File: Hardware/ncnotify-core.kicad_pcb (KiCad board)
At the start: 4 copper layers, 44 x 21 mm, 44 parts, among them J1 BNC5-J-P-GN-RA-BH2D, J2 Conn_ARM_JTAG_SWD_10, J3 USB4110-GF-A, Q1 NX3008NBKS, SW1 SW_Push, SW2 SW_Push, U1 STM32L422CBT6, U2 TLV71333PDBV, U3 USBLC6-2SC6, U4 USBLC6-2SC6, X1 SMTU1632-LF, Y1 Q13FC1350000400

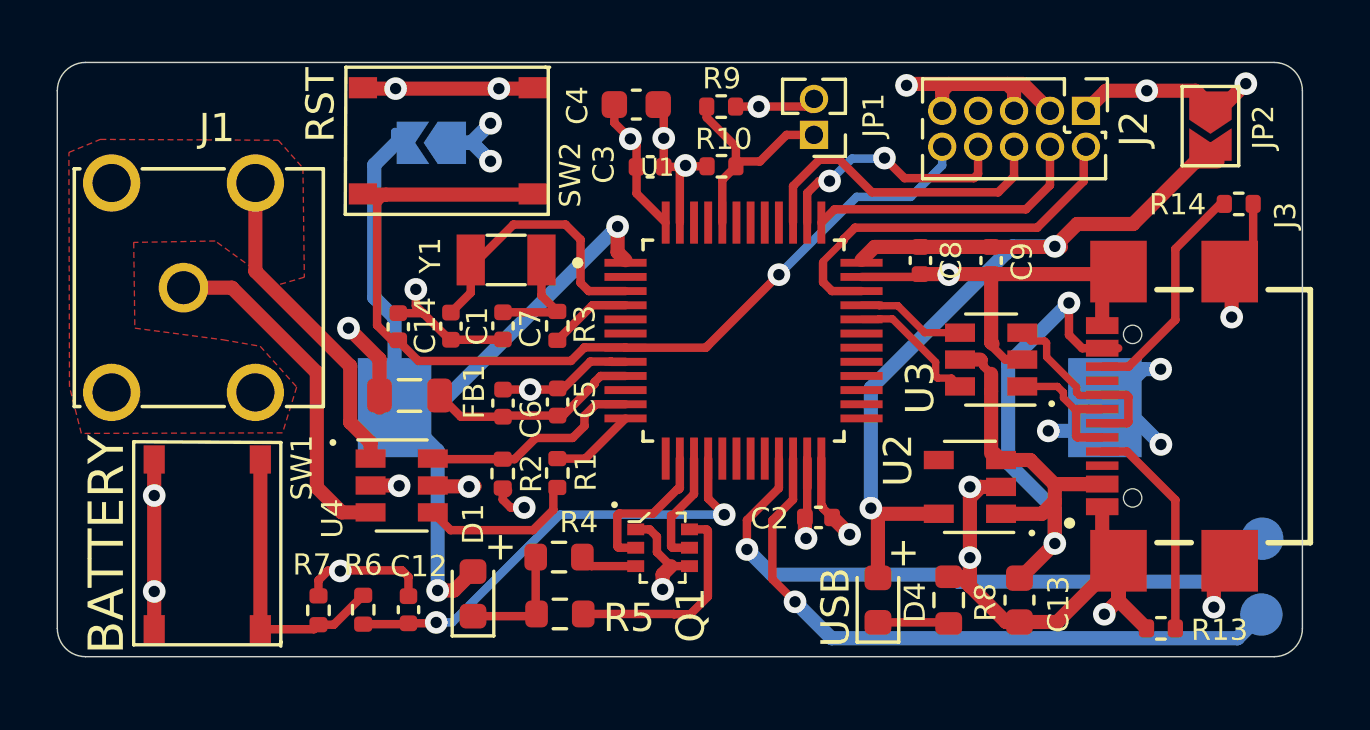
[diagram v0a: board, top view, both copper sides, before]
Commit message: sizeup batt to 2032 for current limit; re-place to fit
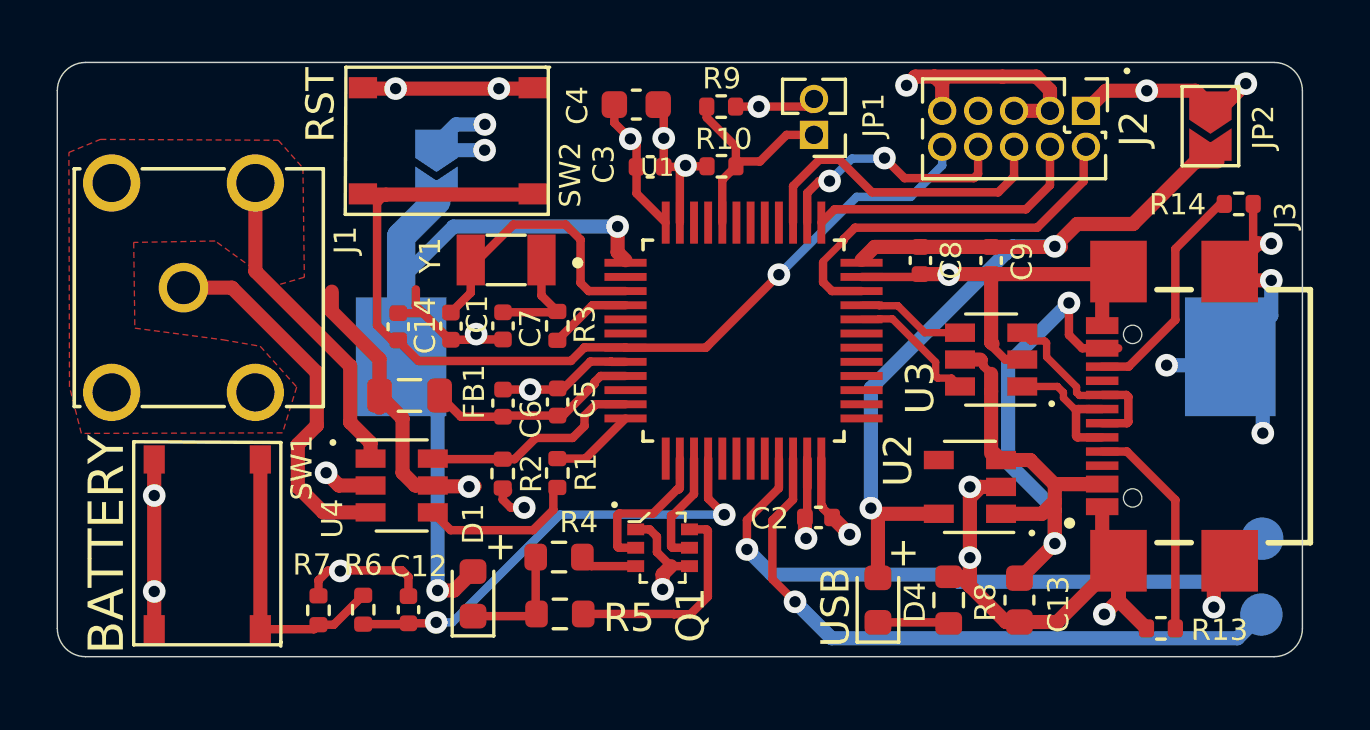
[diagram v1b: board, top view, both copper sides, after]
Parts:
- removed X1: SMTU1632-LF, SamacSys_Parts:SMTU1632LF
- added BT1: BU2032SM-BT-GTR, libs:BAT_BU2032SM-BT-GTR, B.Cu at (235.8, -39.6)
- moved JP3 0.78 mm to (222.4, -46.4), turned to 270 degrees
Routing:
- net GND: track 95.1 -> 104.7 mm
- net VDD: track 32.1 -> 38.4 mm, vias 11 -> 10
- net VBAT: track 31.5 -> 35.2 mm
- net S+: track 12.3 -> 13.2 mm

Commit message: Resolve TH conflicts; add 3d models
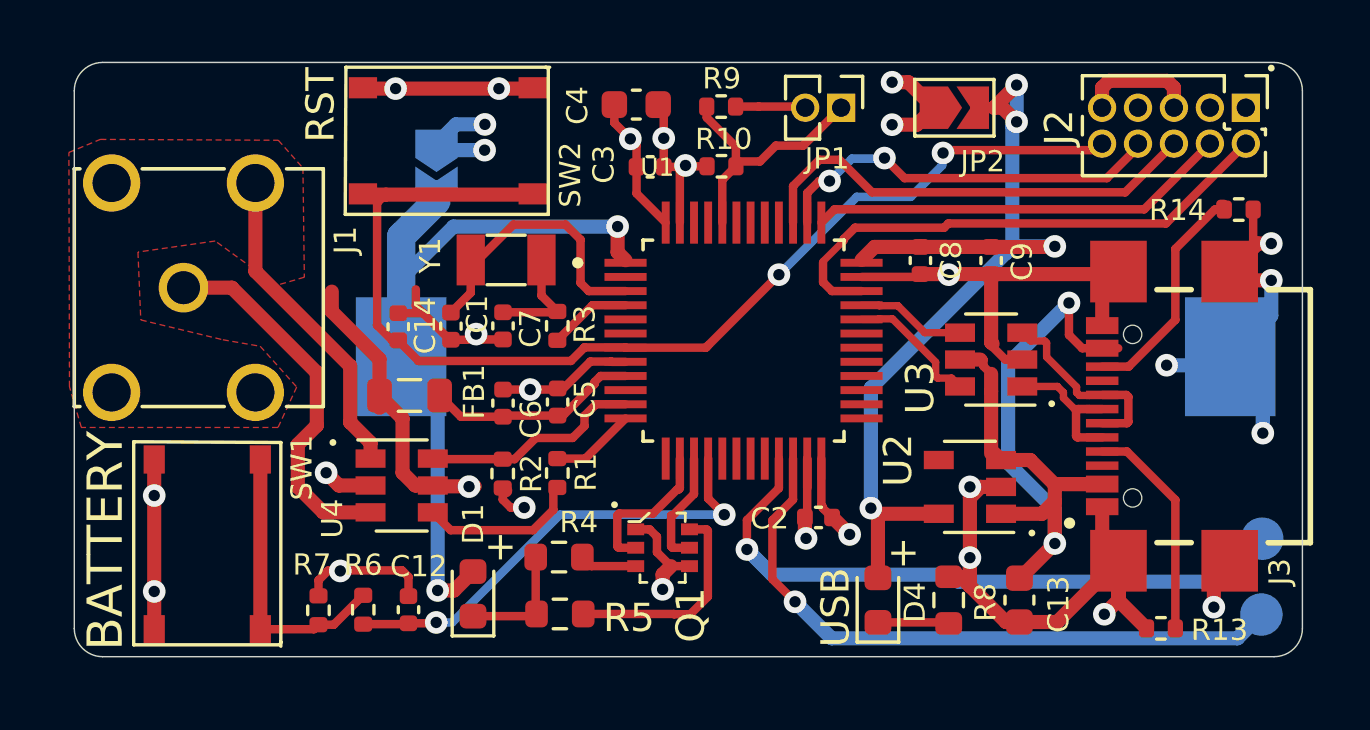
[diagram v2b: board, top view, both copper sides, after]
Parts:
- moved JP2 9.07 mm to (240.7, -48.4), turned to 0 degrees
- moved J2 5.65 mm to (251.0, -48.4)
- moved JP1 1.36 mm to (236.7, -48.4), turned to 270 degrees
- moved R14 0.20 mm to (250.8, -44.8)
- turned BT1 to 0 degrees
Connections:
- BT1 pad +: GND -> VBAT
- BT1 pad -: VBAT -> GND
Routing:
- net NRST: track 34.9 -> 40.6 mm, vias 1 -> 2
- net JTMS-SWDIO: track 13.6 -> 18.9 mm
- net JTDI: track 8.91 -> 14.1 mm
- net JTCK-SWCLK: track 9.73 -> 14.9 mm
- net JTDO: track 11.2 -> 16.3 mm
- net GND: track 104.7 -> 99.6 mm, vias 21 -> 20
- net VDD: track 38.4 -> 35.0 mm, vias 10 -> 9
- net Net-(JP1-Pad1): track 7.84 -> 9.20 mm
- net VBUS: track 33.6 -> 33.5 mm, vias 2 -> 4
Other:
- board size 44 x 21 mm -> 43.4 x 21 mm
- board text added: "v1.1 NCNotify Data Logger Bowen Shaner"
- board text removed: "NCNotify Data Logger v1.1 Bowen Shaner"

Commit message: micro-usb connector
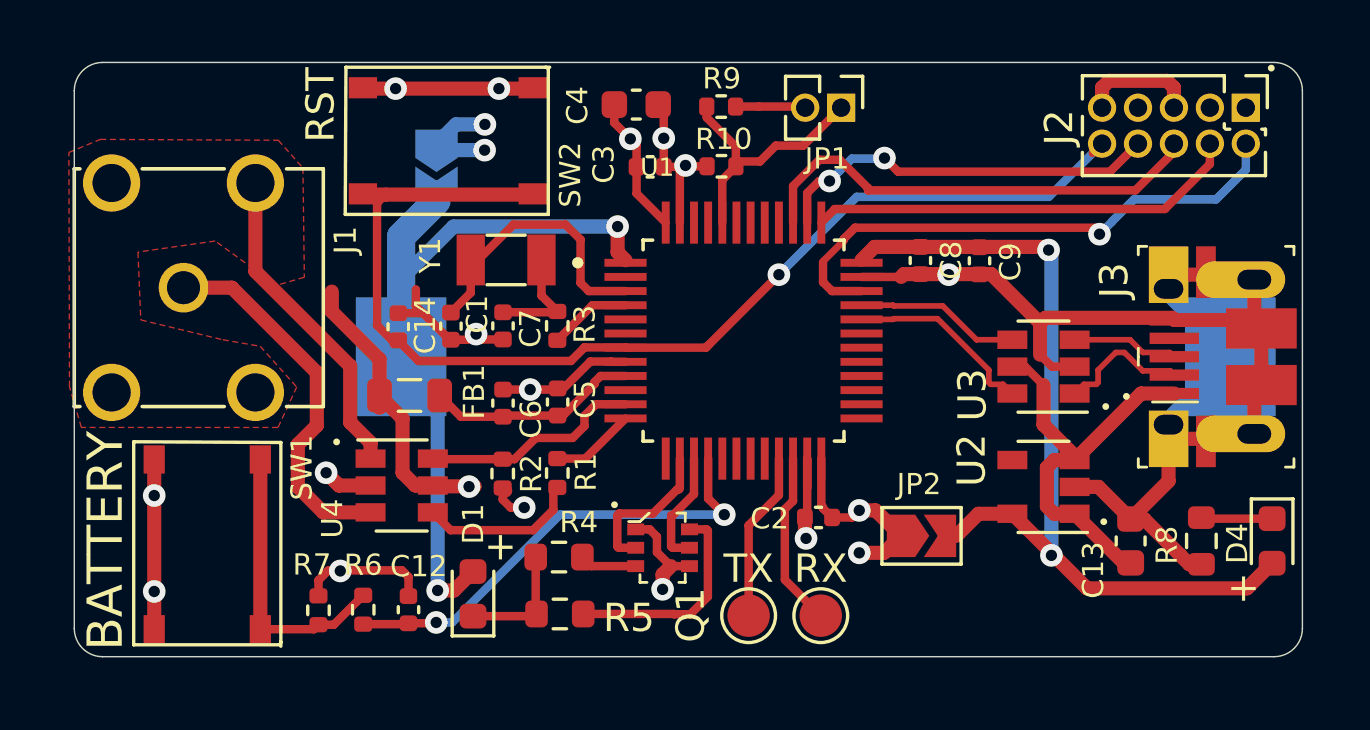
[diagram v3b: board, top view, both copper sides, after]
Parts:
- removed R13, R14: 5k1, Resistor_SMD:R_0402_1005Metric
- removed TP1: TestPoint, TestPoint:TestPoint_Pad_D1.5mm
- added TPE: TestPoint, TestPoint:TestPoint_Pad_D1.5mm, F.Cu at (236.0, -30.4)
- J3: value USB4110-GF-A -> 10103594-0001LF; footprint libs:GCT_USB4110-GF-A -> digikey-footprints:USB_Micro_B_Female_10103594-0001LF
- TP2: moved to F.Cu
- moved TP2 18.4 mm to (233.4, -30.4), turned to 90 degrees
- moved JP2 15.2 mm to (239.5, -33.3)
- moved D4 14.1 mm to (251.9, -33.1), turned to 270 degrees
- moved R8 9.17 mm to (249.4, -33.1), turned to 270 degrees
- moved J3 4.79 mm to (251.3, -39.6)
- moved C13 4.45 mm to (246.9, -33.1), turned to 90 degrees
- moved U2 2.60 mm to (243.8, -35.0)
- moved U3 1.87 mm to (243.8, -39.2)
- moved C9 0.41 mm to (241.6, -43.0)
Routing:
- net USART3_TX: track 23.0 -> 5.99 mm, vias 1 -> 0
- net USART3_RX: track 23.1 -> 6.20 mm, vias 1 -> 0
- net VUSB: track 29.7 -> 15.3 mm, vias 2 -> 0
- net Net-(J3-PadB5): track 8.22 -> 0.00 mm
- net Net-(J3-PadA5): track 7.83 -> 0.00 mm
- net CONN_D+: track 6.94 -> 3.77 mm
- net VBUS: track 33.5 -> 31.1 mm, vias 4 -> 2
- net D+: track 3.88 -> 5.84 mm
- net D-: track 4.77 -> 6.70 mm
- net CONN_D-: track 6.05 -> 4.72 mm
- net GND: track 99.6 -> 98.7 mm, vias 20 -> 12
- net JTMS-SWDIO: track 18.9 -> 19.6 mm, vias 0 -> 1
- net VDD: track 35.0 -> 35.2 mm, vias 9 -> 8
- net NRST: track 40.6 -> 40.7 mm, vias 2 -> 1
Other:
- board text added: "v1.1 B. Shaner NCNotify Data Logger"
- board text removed: "USB"
- board text removed: "v1.1 NCNotify Data Logger Bowen Shaner"
